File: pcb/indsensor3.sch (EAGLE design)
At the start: 35 parts, among them U1 AD8221ARMZ, U2 AD8646ARMZ, U3 AD8310ARMZ

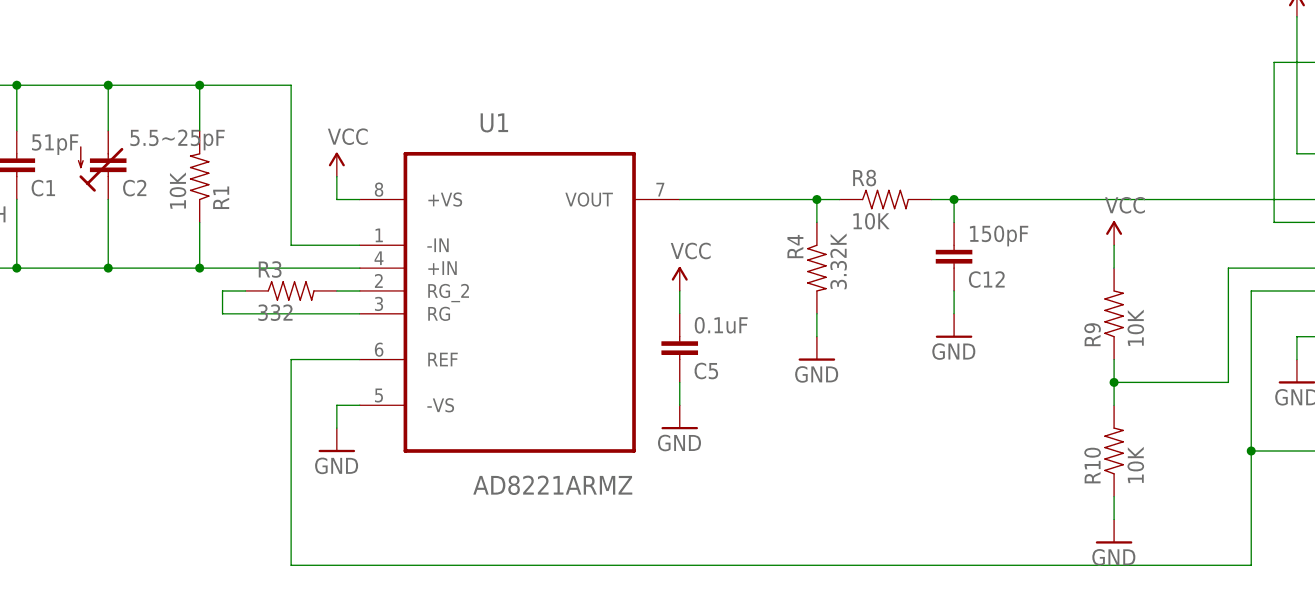
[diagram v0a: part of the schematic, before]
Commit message: Updated component values
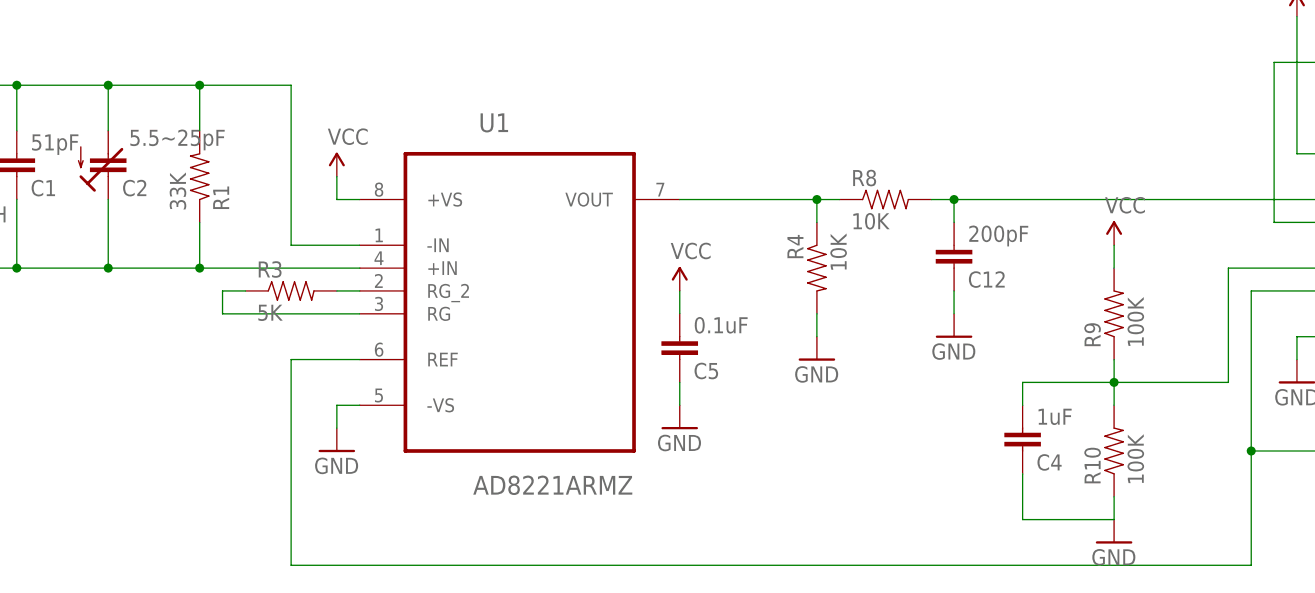
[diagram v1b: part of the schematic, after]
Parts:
- added C4: 1uF, SparkFun-Capacitors:CAP0603-CAP
- C12: value 150pF -> 200pF
- R1: value 10K -> 33K
- R10, R9: value 10K -> 100K
- R3: value 332 -> 5K
- R4: value 3.32K -> 10K
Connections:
- net GND: now also C4.1
- net N$13: now also C4.2
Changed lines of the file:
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@@
 <part name="C7" library="SparkFun-Capacitors" deviceset="CAP" device="0603-CAP" value="10nF"/>
 <part name="C8" library="SparkFun-Capacitors" deviceset="CAP" device="0603-CAP" value="10nF"/>
-<part name="R1" library="SparkFun-Resistors" deviceset="RESISTOR" device="0603" value="10K"/>
-<part name="R3" library="SparkFun-Resistors" deviceset="RESISTOR" device="0603" value="332"/>
+<part name="R1" library="SparkFun-Resistors" deviceset="RESISTOR" device="0603" value="33K"/>
+<part name="R3" library="SparkFun-Resistors" deviceset="RESISTOR" device="0603" value="5K"/>
 <part name="R5" library="SparkFun-Resistors" deviceset="RESISTOR" device="0603" value="1K"/>
 <part name="C9" library="SparkFun-Capacitors" deviceset="CAP" device="0603-CAP" value="10nF"/>
@@
 <part name="R2" library="SparkFun-Resistors" deviceset="RESISTOR" device="0603" value="100K"/>
 <part name="GND11" library="SparkFun-Aesthetics" deviceset="GND" device=""/>
-<part name="R4" library="SparkFun-Resistors" deviceset="RESISTOR" device="0603" value="3.32K"/>
+<part name="R4" library="SparkFun-Resistors" deviceset="RESISTOR" device="0603" value="10K"/>
 <part name="GND12" library="SparkFun-Aesthetics" deviceset="GND" device=""/>
 <part name="GND4" library="SparkFun-Aesthetics" deviceset="GND" device=""/>
@@
 <part name="U2" library="ADI-Phase-2" deviceset="AD8646ARMZ" device=""/>
 <part name="R8" library="SparkFun-Resistors" deviceset="RESISTOR" device="0603" value="10K"/>
-<part name="C12" library="SparkFun-Capacitors" deviceset="CAP" device="0603-CAP" value="150pF"/>
+<part name="C12" library="SparkFun-Capacitors" deviceset="CAP" device="0603-CAP" value="200pF"/>
 <part name="GND14" library="SparkFun-Aesthetics" deviceset="GND" device=""/>
 <part name="SUPPLY4" library="SparkFun-Aesthetics" deviceset="VCC" device=""/>
@@
 <part name="GND17" library="SparkFun-Aesthetics" deviceset="GND" device=""/>
 <part name="SUPPLY7" library="SparkFun-Aesthetics" deviceset="VCC" device=""/>
-<part name="R9" library="SparkFun-Resistors" deviceset="RESISTOR" device="0603" value="10K"/>
-<part name="R10" library="SparkFun-Resistors" deviceset="RESISTOR" device="0603" value="10K"/>
+<part name="R9" library="SparkFun-Resistors" deviceset="RESISTOR" device="0603" value="100K"/>
+<part name="R10" library="SparkFun-Resistors" deviceset="RESISTOR" device="0603" value="100K"/>
 <part name="GND5" library="SparkFun-Aesthetics" deviceset="GND" device=""/>
 <part name="SUPPLY8" library="SparkFun-Aesthetics" deviceset="VCC" device=""/>
@@
 <part name="U$7" library="Custom" deviceset="SHIELD-MIDDLEPART" device=""/>
 <part name="U$8" library="Custom" deviceset="SHIELD-MIDDLE3" device=""/>
+<part name="C4" library="SparkFun-Capacitors" deviceset="CAP" device="0603-CAP" value="1uF"/>
 </parts>
 <sheets>
@@
 <instance part="U$7" gate="G$1" x="144.78" y="111.76"/>
 <instance part="U$8" gate="G$1" x="144.78" y="132.08"/>
+<instance part="C4" gate="G$1" x="114.3" y="35.56" rot="MR180"/>
 </instances>
 <busses>
@@
 <pinref part="GND5" gate="1" pin="GND"/>
 <wire x1="124.46" y1="25.4" x2="124.46" y2="27.94" width="0.1524" layer="91"/>
+<pinref part="C4" gate="G$1" pin="1"/>
+<wire x1="114.3" y1="30.48" x2="114.3" y2="25.4" width="0.1524" layer="91"/>
+<wire x1="114.3" y1="25.4" x2="124.46" y2="25.4" width="0.1524" layer="91"/>
 </segment>
 </net>
@@
 <pinref part="U2" gate="A" pin="+IN_B"/>
 <wire x1="147.32" y1="53.34" x2="137.16" y2="53.34" width="0.1524" layer="91"/>
-</segment>
-</net>
+<pinref part="C4" gate="G$1" pin="2"/>
+<wire x1="114.3" y1="38.1" x2="114.3" y2="40.64" width="0.1524" layer="91"/>
+<wire x1="114.3" y1="40.64" x2="124.46" y2="40.64" width="0.1524" layer="91"/>
+</segment>
+</net>

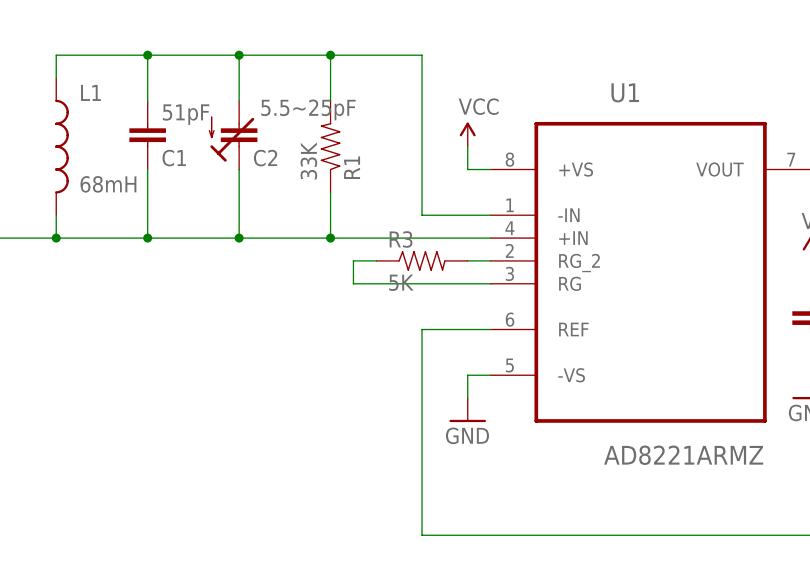
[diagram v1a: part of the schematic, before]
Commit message: Changed gain resistor
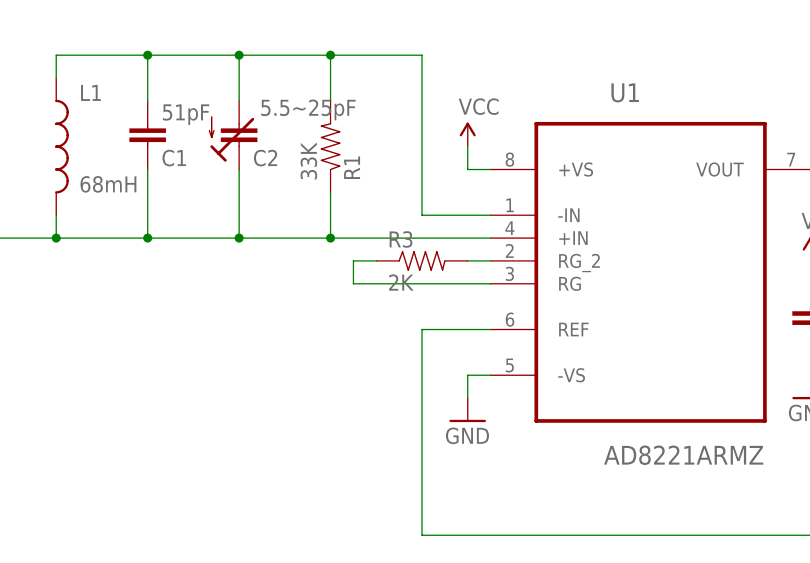
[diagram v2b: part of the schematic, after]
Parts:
- R3: value 5K -> 2K
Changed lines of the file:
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@@
 <part name="C8" library="SparkFun-Capacitors" deviceset="CAP" device="0603-CAP" value="10nF"/>
 <part name="R1" library="SparkFun-Resistors" deviceset="RESISTOR" device="0603" value="33K"/>
-<part name="R3" library="SparkFun-Resistors" deviceset="RESISTOR" device="0603" value="5K"/>
+<part name="R3" library="SparkFun-Resistors" deviceset="RESISTOR" device="0603" value="2K"/>
 <part name="R5" library="SparkFun-Resistors" deviceset="RESISTOR" device="0603" value="1K"/>
 <part name="C9" library="SparkFun-Capacitors" deviceset="CAP" device="0603-CAP" value="10nF"/>
